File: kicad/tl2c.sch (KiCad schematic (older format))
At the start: 0 parts

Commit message: Started the schematic
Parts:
- added C?: 1μF 25V, symbol C
- added C?: 1μF 16V, symbol C
- added C?: 100n 10V, symbol C
- added D?: LED, symbol LED
- added D? (x3): D, symbol D
- added IC?: ATTINY20-X, TSSOP14, symbol ATTINY20-X
- added P?: ISP Header, symbol CONN_02X03
- added P?: I2C Master, symbol CONN_01X03
- added P?: CONN_01X04, symbol CONN_01X04
- added P?: 240VAC, symbol CONN_01X02
- added P?: 12VDC, symbol CONN_01X02
- added R?: 0Ω, symbol R
- added R?: 660Ω, symbol R
- added R?: 10kΩ, symbol R
- added R? (x2): 330Ω, symbol R
- added R? (x2): NOPOP, symbol R
- added REL? (x2): Relay_UG, symbol Relay_JW1AFSN12F
- added REL? (x2): Relay_EG, symbol Relay_JW1AFSN12F
- added REL? (x2): Relay_OG, symbol Relay_JW1AFSN12F
- added U?: LS2979M33TR, symbol LS2979M33TR
- added W? (x2): TEST_1P, symbol TEST_1P
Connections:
- net labels added: GND, Lin, LineEG, LineOG, LineUG, MISO, MOSI, Neutral, PIR_EG, PIR_OG, PIR_UG, RelayEG, RelayOG, RelayUG, Reset, SCK, SCL, SDA, SLC, Spare1, Spare2, U+, Ub+
- wire segments 0 -> 83
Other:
- note added: "TODO - Verify if the Maximum voltage is \na safe limit for this usage of 12V Vin"
- note added: "We have a 3V3 system \nand possibly a 5V programmer. \nInitial research suggests the AVRISP MkII\ncan drive ISP lines at the required voltage.\nhttps://forum.arduino.cc/index.php?topic=92544.0"

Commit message: Completed the initial schematic
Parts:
- removed P?: CONN_01X04, symbol CONN_01X04
- added P2: Spare, symbol CONN_01X02
- added P6: LED Driver, symbol CONN_01X06
- added P7: PIR13, symbol CONN_01X09
- added Q1, Q2, Q3: IRLML2502, Micro3, symbol IRLML2502
- added R10, R8, R9: 10kΩ, symbol R
- added SW1: Reset, symbol SW_PUSH
- gave numbers to parts that had none: 25
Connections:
- net labels removed: SLC
- wire segments 83 -> 113
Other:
- note added: "TODO - Verify the values \nof the resistors for sharing\nthe IO lines."
- note added: "TODO - Will these MOSFETs \nbe in spec?"
- moved on the sheet: C1, C2, C3, D1, D2, D3, D4, IC1, P1, P3, P4, R1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

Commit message: Changes to the schematic after a review - added further test points and LEDs
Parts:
- removed C1: 1μF 25V, symbol C
- removed C3: 1μF 16V, symbol C
- removed D1: LED, symbol LED
- removed D2, D3, D4: D, symbol D
- removed P1: 12VDC, symbol CONN_01X02
- removed P7: PIR13, symbol CONN_01X09
- removed Q1, Q2, Q3: IRLML2502, Micro3, symbol IRLML2502
- removed R1: 0Ω, symbol R
- removed R10, R8, R9: 10kΩ, symbol R
- removed R3: 660Ω, symbol R
- removed unit 1 of REL1
- removed unit 1 of REL2
- removed unit 1 of REL3
- removed U1: LS2979M33TR, symbol LS2979M33TR
- removed W1, W2: TEST_1P, symbol TEST_1P
- added P101: 12VDC, symbol CONN_01X02
- added TP101: TPSCL, symbol TEST_1P
- added TP102: TPSDA, symbol TEST_1P
- added TP103: TPGND, symbol TEST_1P
- IC101: renamed from IC1; MFP (none) -> ATTINY20-SSUR
- REL101: renamed from REL1; MFP (none) -> JW1AFSN-12-F
- REL102: renamed from REL2; MFP (none) -> JW1AFSN-12-F
- REL103: renamed from REL3; MFP (none) -> JW1AFSN-12-F
- renumbered C2 to C101, P2 to P102, P3 to P103, P4 to P104, P5 to P105, P6 to P106, R2 to R101, R4 to R102, R5 to R103, R6 to R104, R7 to R105, SW1 to SW101
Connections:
- net labels added: SIG_EG, SIG_OG, SIG_UG
- net labels removed: PIR_EG, PIR_OG, PIR_UG
- wire segments 113 -> 71
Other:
- note added: "240VAC - What needs to be considered\nfor the layout here?\n - Track witdth, thickness, spacing.\n - Interference"
- note added: "The RP has 1k8Ω pullup\nresistors to 3V3\n"
- note removed: "TODO - Verify if the Maximum voltage is \na safe limit for this usage of 12V Vin"
- note removed: "TODO - Will these MOSFETs \nbe in spec?"
- moved on the sheet: C101, IC101, P102, P103, R101, R102, R103, R104, R105, REL101B, REL102B, REL103B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

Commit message: Started assigning foot prints to the parts
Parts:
- added P105, P107: LED_DRIVER, Pin_Headers:Pin_Header_Straight_1x05, symbol CONN_01X05
- C101: footprint (none) -> Capacitors_SMD:C_0805
- IC101: footprint TSSOP14 -> Housings_SOIC:SOIC-14_3.9x8.7mm_Pitch1.27mm; Conrad-PN (none) -> 1267295 - 62; Digikey-PN (none) -> ATTINY20-SSURCT-ND
- P101: footprint (none) -> Pin_Headers:Pin_Header_Straight_1x02; Conrad-PN (none) -> Value; Digikey-PN (none) -> Value; MFP (none) -> Value
- P102: renamed from P103; footprint (none) -> Pin_Headers:Pin_Header_Straight_1x03; Conrad-PN (none) -> Value; Digikey-PN (none) -> Value; MFP (none) -> Value
- P103: renamed from P102; footprint (none) -> Pin_Headers:Pin_Header_Straight_1x02; Conrad-PN (none) -> Value; Digikey-PN (none) -> Value; MFP (none) -> Value
- P104: footprint (none) -> Pin_Headers:Pin_Header_Straight_2x03; Conrad-PN (none) -> Value; Digikey-PN (none) -> Value; MFP (none) -> Value
- P106: renamed from P105; Conrad-PN (none) -> Value; Digikey-PN (none) -> Value; MFP (none) -> Value
- P108: renamed from P106; value LED Driver -> LED_OUT
- R101, R102, R103, R104, R105: footprint (none) -> Resistors_SMD:R_0805
- TP101: renamed from TP103; footprint (none) -> Measurement_Points:Measurement_Point_Round-SMD-Pad_Small
- TP102: renamed from TP101; footprint (none) -> Measurement_Points:Measurement_Point_Round-SMD-Pad_Small
- TP103: renamed from TP102; footprint (none) -> Measurement_Points:Measurement_Point_Round-SMD-Pad_Small
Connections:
- net GND: now also P105.5 (P5), P107.5 (P5)
- net RelayEG: now also P105.3 (P3), P107.3 (P3)
- net RelayOG: now also P105.4 (P4), P107.4 (P4)
- net RelayUG: now also P105.2 (P2), P107.2 (P2)
- net U+: now also P107.1 (P1)
- net Ub+: now also P105.1 (P1)
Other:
- note added: "240V AC Board"
- note removed: "240VAC - What needs to be considered\nfor the layout here?\n - Track witdth, thickness, spacing.\n - Interference"
- moved on the sheet: P104, P106, P108, REL101B, REL102B, REL103B

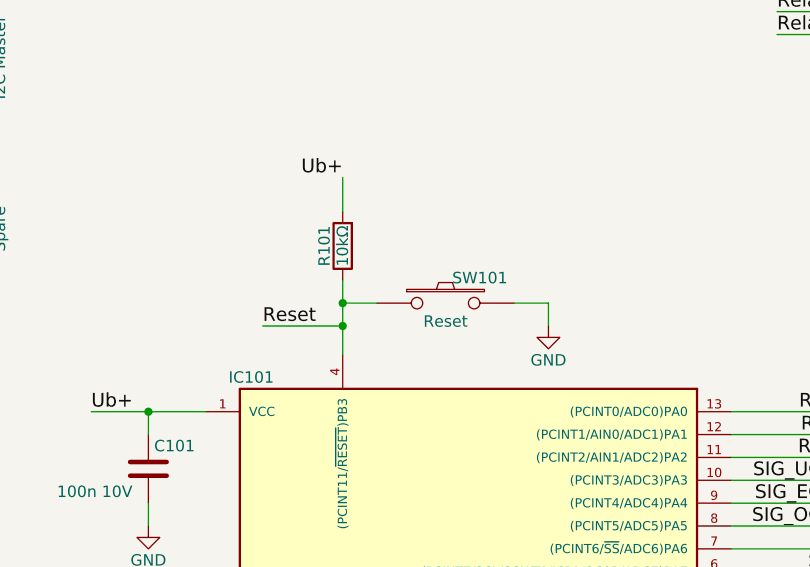
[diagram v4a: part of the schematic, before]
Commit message: Added more footprints to the parts
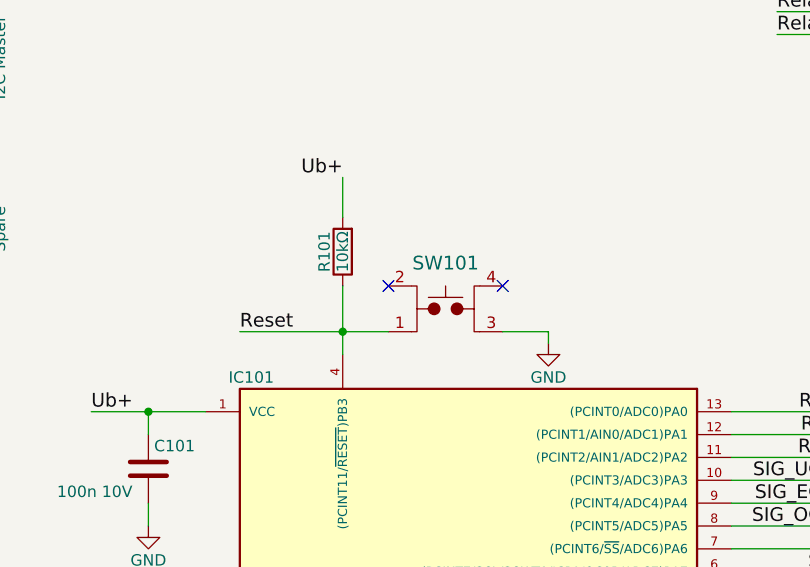
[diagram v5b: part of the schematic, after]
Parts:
- removed SW101: Reset, symbol SW_PUSH
- added SW101: TL3315NF160Q, tl2c-footprint:PTS525SM15SMTR2LFS, symbol TL3315NF160Q
- REL101, REL102, REL103: footprint (none) -> tl2c-footprint:JW1AFSN-12-F; Conrad-PN (none) -> Value; Digikey-PN (none) -> Value
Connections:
- net GND: now also SW101.3
- net Reset: now also SW101.1
- no-connect marks 0 -> 2
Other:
- moved on the sheet: R101
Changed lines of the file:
@@
 L R R101
 U 1 1 584C40A0
-P 3700 3875
-F 0 "R101" V 3780 3875 50  0000 C CNN
-F 1 "10kΩ" V 3700 3875 50  0000 C CNN
-F 2 "Resistors_SMD:R_0805" V 3630 3875 50  0001 C CNN
-F 3 "" H 3700 3875 50  0000 C CNN
-	1    3700 3875
+P 3700 3900
+F 0 "R101" V 3780 3900 50  0000 C CNN
+F 1 "10kΩ" V 3700 3900 50  0000 C CNN
+F 2 "Resistors_SMD:R_0805" V 3630 3900 50  0001 C CNN
+F 3 "" H 3700 3900 50  0000 C CNN
+	1    3700 3900
 	-1   0    0    1
 $EndComp
@@
 Text Label 3700 3575 2    60   ~ 0
 Ub+
-Text Label 3350 4225 0    60   ~ 0
-Reset
 Text Label 5900 5300 2    60   ~ 0
 SCK
@@
 F 0 "REL101" H 8050 1050 60  0000 C CNN
 F 1 "Relay_UG" H 8060 1280 60  0000 C CNN
-F 2 "" H 7920 1140 60  0001 C CNN
+F 2 "tl2c-footprint:JW1AFSN-12-F" H 7920 1140 60  0001 C CNN
 F 3 "" H 7920 1140 60  0000 C CNN
 F 4 "JW1AFSN-12-F" H 8050 1150 60  0001 C CNN "MFP"
+F 5 "Value" H 8050 1150 60  0001 C CNN "Conrad-PN"
+F 6 "Value" H 8050 1150 60  0001 C CNN "Digikey-PN"
 	2    8050 1150
 	1    0    0    -1
@@
 F 0 "REL102" H 8070 1410 60  0000 C CNN
 F 1 "Relay_EG" H 8060 1680 60  0000 C CNN
-F 2 "" H 7920 1540 60  0001 C CNN
+F 2 "tl2c-footprint:JW1AFSN-12-F" H 7920 1540 60  0001 C CNN
 F 3 "" H 7920 1540 60  0000 C CNN
 F 4 "JW1AFSN-12-F" H 8050 1550 60  0001 C CNN "MFP"
+F 5 "Value" H 8050 1550 60  0001 C CNN "Conrad-PN"
+F 6 "Value" H 8050 1550 60  0001 C CNN "Digikey-PN"
 	2    8050 1550
 	1    0    0    -1
@@
 F 0 "REL103" H 8070 1860 60  0000 C CNN
 F 1 "Relay_OG" H 8060 2130 60  0000 C CNN
-F 2 "" H 7920 1990 60  0001 C CNN
+F 2 "tl2c-footprint:JW1AFSN-12-F" H 7920 1990 60  0001 C CNN
 F 3 "" H 7920 1990 60  0000 C CNN
 F 4 "JW1AFSN-12-F" H 8050 2000 60  0001 C CNN "MFP"
+F 5 "Value" H 8050 2000 60  0001 C CNN "Conrad-PN"
+F 6 "Value" H 8050 2000 60  0001 C CNN "Digikey-PN"
 	2    8050 2000
 	1    0    0    -1
@@
 Neutral
 $Comp
-L SW_PUSH SW101
-U 1 1 584CAACE
-P 4150 4125
-F 0 "SW101" H 4300 4235 50  0000 C CNN
-F 1 "Reset" H 4150 4045 50  0000 C CNN
-F 2 "" H 4150 4125 50  0001 C CNN
-F 3 "" H 4150 4125 50  0000 C CNN
-	1    4150 4125
-	1    0    0    -1
-$EndComp
-$Comp
 L GND #PWR06
 U 1 1 584CB28B
-P 4600 4225
-F 0 "#PWR06" H 4600 3975 50  0001 C CNN
-F 1 "GND" H 4600 4075 50  0000 C CNN
-F 2 "" H 4600 4225 50  0000 C CNN
-F 3 "" H 4600 4225 50  0000 C CNN
-	1    4600 4225
+P 4600 4300
+F 0 "#PWR06" H 4600 4050 50  0001 C CNN
+F 1 "GND" H 4600 4150 50  0000 C CNN
+F 2 "" H 4600 4300 50  0000 C CNN
+F 3 "" H 4600 4300 50  0000 C CNN
+	1    4600 4300
 	1    0    0    -1
 $EndComp
@@
 	2850 5000 2850 5100
 Wire Wire Line
-	3700 4025 3700 4350
-Wire Wire Line
-	3700 3725 3700 3575
-Wire Wire Line
-	3700 4225 3350 4225
-Connection ~ 3700 4225
+	3700 3575 3700 3750
 Wire Wire Line
 	3700 6050 3700 6200
@@
 	1900 3850 1500 3850
 Wire Wire Line
-	3700 4125 3850 4125
-Connection ~ 3700 4125
-Wire Wire Line
-	4450 4125 4600 4125
-Wire Wire Line
-	4600 4125 4600 4225
+	4400 4250 4600 4250
+Wire Wire Line
+	4600 4250 4600 4300
 Wire Wire Line
 	1450 1350 1750 1350
@@
 Wire Notes Line
 	7150 3050 6550 3050
+$Comp
+L TL3315NF160Q SW101
+U 1 1 58559EF5
+P 4150 4150
+F 0 "SW101" V 4350 4150 60  0000 C CNN
+F 1 "TL3315NF160Q" H 4600 4200 60  0001 C CNN
+F 2 "tl2c-footprint:PTS525SM15SMTR2LFS" H 4150 4100 60  0001 C CNN
+F 3 "" H 4150 4100 60  0000 C CNN
+F 4 "Value" H 4150 4150 60  0001 C CNN "MFP"
+F 5 "Value" H 4150 4150 60  0001 C CNN "Conrad-PN"
+F 6 "Value" H 4150 4150 60  0001 C CNN "Digikey-PN"
+	1    4150 4150
+	0    -1   -1   0
+$EndComp
+Wire Wire Line
+	3700 4050 3700 4350
+Wire Wire Line
+	3250 4250 3900 4250
+Connection ~ 3700 4250
+Text Label 3250 4250 0    60   ~ 0
+Reset
+NoConn ~ 3900 4050
+NoConn ~ 4400 4050
 $EndSCHEMATC

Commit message: Provided a place holder connector for the 240V side and started the layout
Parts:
- P106: footprint (none) -> tl2c-footprint:Pin_Header_1_x_2_5mmPitch
- P108: footprint (none) -> tl2c-footprint:Pin_Header_1_x_6_54mmPitch
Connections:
- net RelayEG: no longer P107.3 (P3)
- net RelayOG: no longer P107.4 (P4)
- net RelayUG: no longer P107.2 (P2)
- new net LED Driver/Relay_EG: P107.3 (P3)
- new net LED Driver/Relay_OG: P107.2 (P2)
- new net LED Driver/Relay_UG: P107.4 (P4)
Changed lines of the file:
@@
 F 0 "P106" H 6950 1350 50  0000 C CNN
 F 1 "240VAC" V 7050 1200 50  0000 C CNN
-F 2 "" H 6950 1200 50  0001 C CNN
+F 2 "tl2c-footprint:Pin_Header_1_x_2_5mmPitch" H 6950 1200 50  0001 C CNN
 F 3 "" H 6950 1200 50  0000 C CNN
 F 4 "Value" H 6950 1200 60  0001 C CNN "MFP"
@@
 F 0 "P108" H 9950 1750 50  0000 C CNN
 F 1 "LED_OUT" V 10050 1400 50  0000 C CNN
-F 2 "" H 9950 1400 50  0001 C CNN
+F 2 "tl2c-footprint:Pin_Header_1_x_6_54mmPitch" H 9950 1400 50  0001 C CNN
 F 3 "" H 9950 1400 50  0000 C CNN
 	1    9950 1400
@@
 Text Label 8050 2650 0    60   ~ 0
 U+
-Text Label 8050 3000 0    60   ~ 0
-RelayUG
-Text Label 8050 3200 0    60   ~ 0
-RelayEG
-Text Label 8050 3400 0    60   ~ 0
-RelayOG
 Wire Wire Line
 	2600 4600 3100 4600
